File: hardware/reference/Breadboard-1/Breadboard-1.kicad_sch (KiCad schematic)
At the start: 59 parts, among them J1 Left, J2 Right, J3 ICSP, J4 USB_B_Micro, Q31 HSM0903, Q32 HSM0903, Q41 2N7002, Q42 2N7002, Q43 2N7002, U11 AMS1117-5.0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

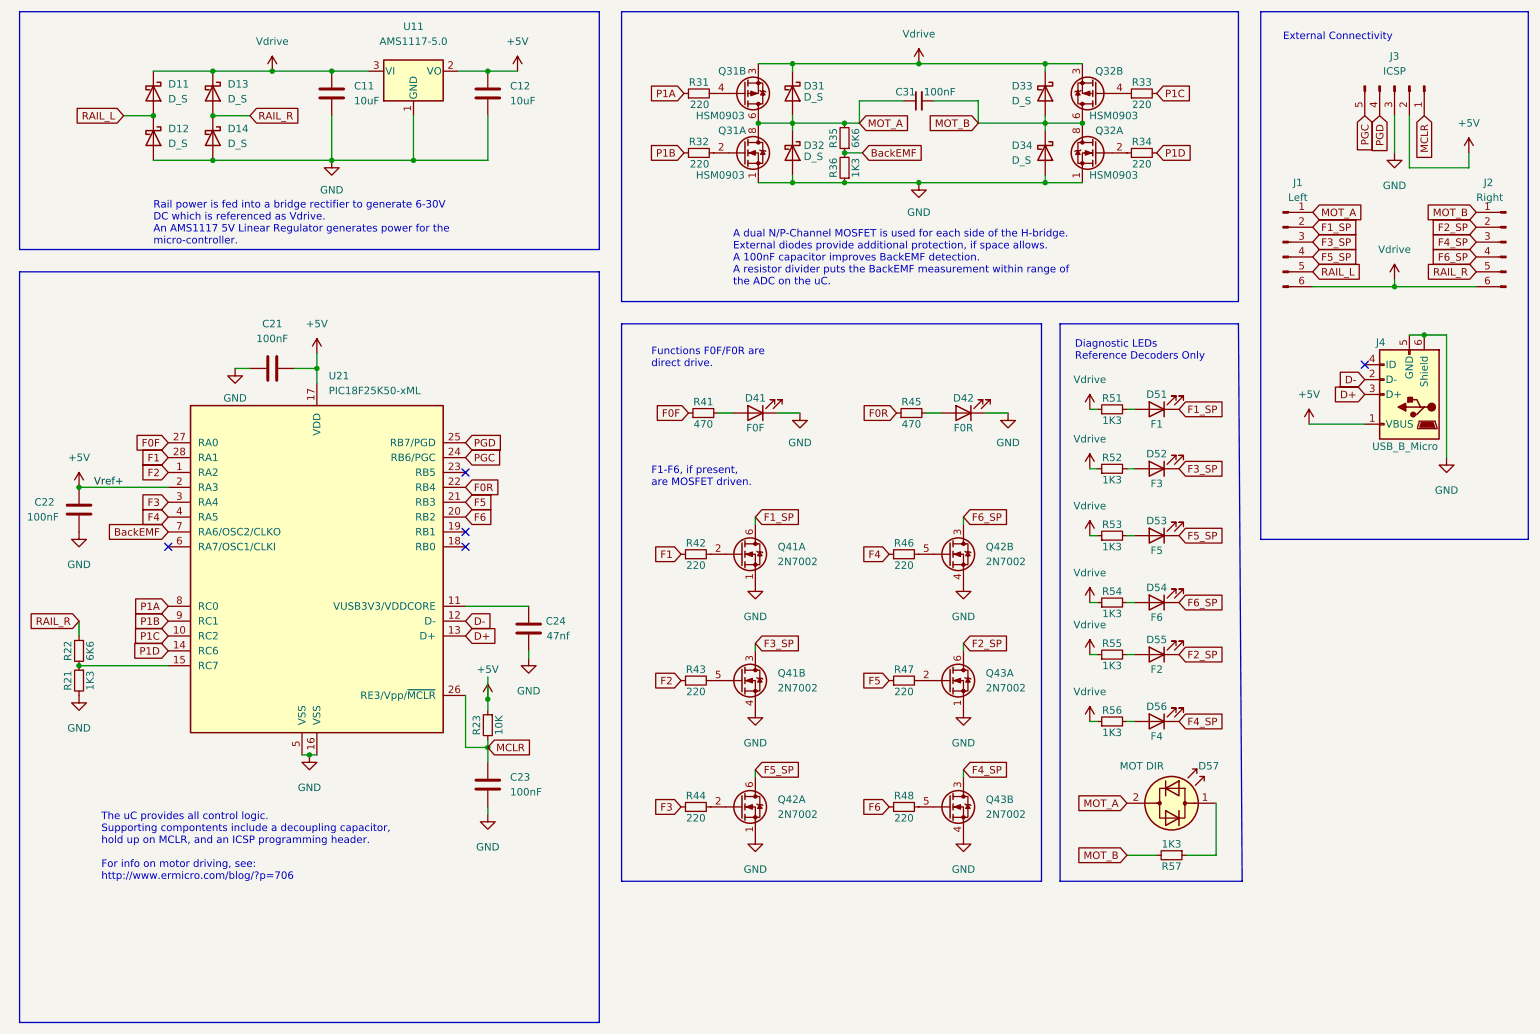
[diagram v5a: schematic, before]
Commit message: Chip selection update, new symbols, improved reference design.
Updated the chip selection document based on availability.

Added new symbols for the chips in the chip selection document.

Switched the reference design to an SSOP-20 package and improved the
layout in general.
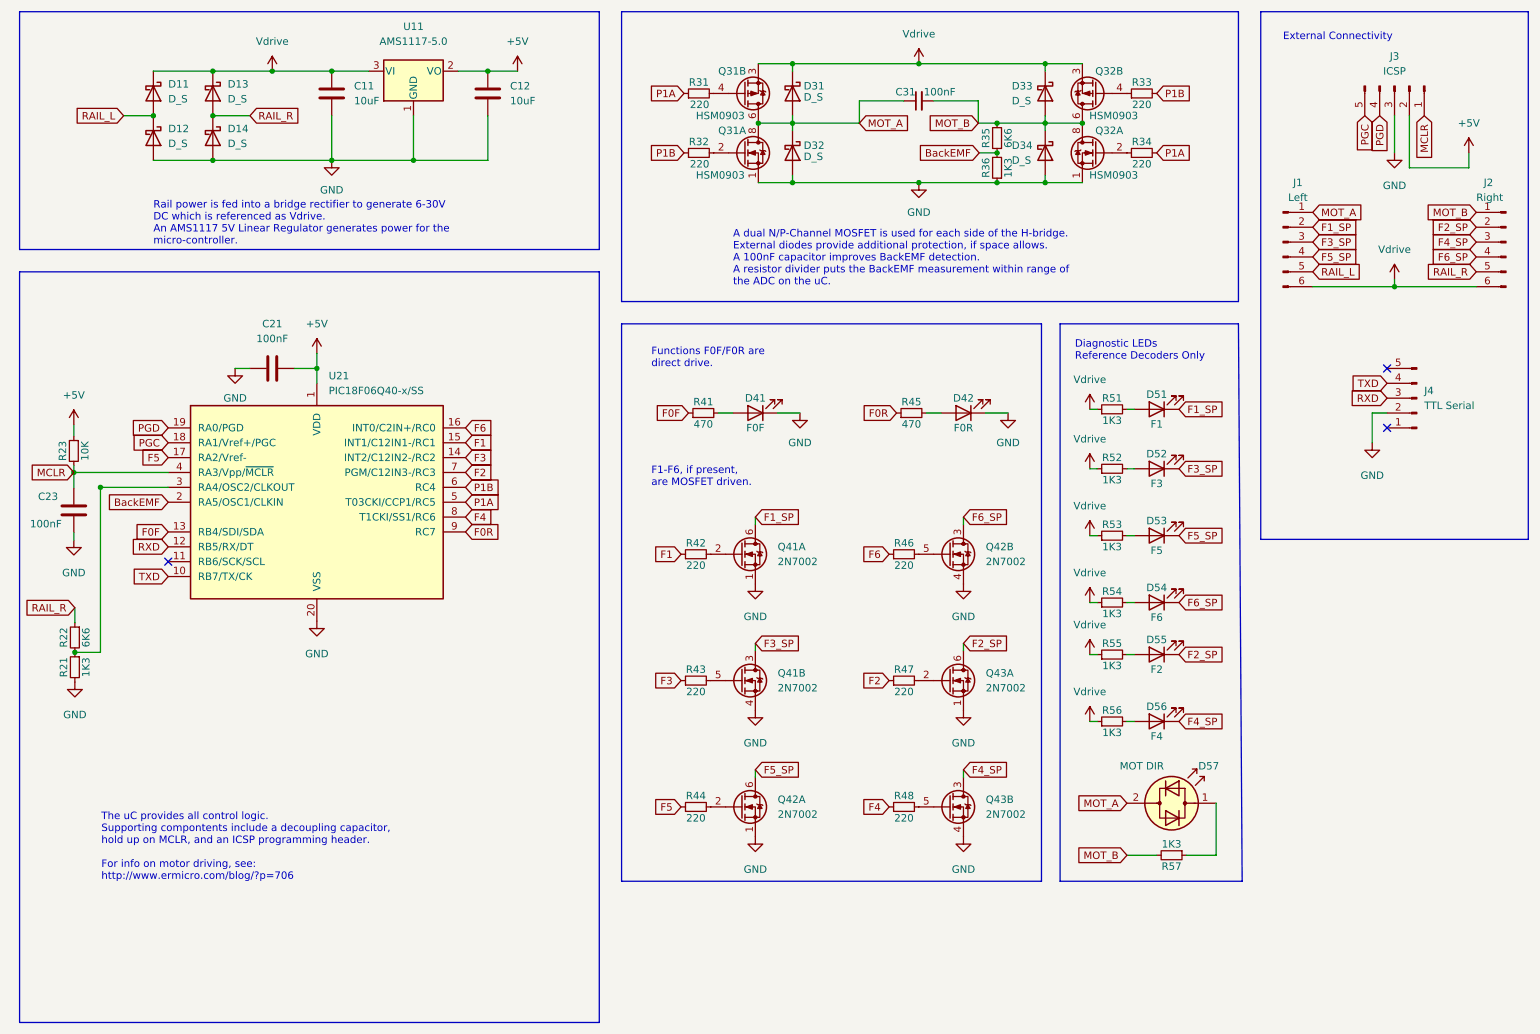
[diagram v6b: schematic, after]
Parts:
- removed C22: 100nF, Capacitor_SMD:C_0402_1005Metric, symbol Device:C
- removed C24: 47nf, Capacitor_SMD:C_0402_1005Metric, symbol Device:C
- removed J4: USB_B_Micro, Connector_USB:USB_Micro-B_Wuerth_629105150521, symbol Connector:USB_B_Micro
- removed U21: PIC18F25K50-xML, Package_DFN_QFN:QFN-28-1EP_6x6mm_P0.65mm_EP4.25x4.25mm, symbol MCU_Microchip_PIC18:PIC18F25K50-xML
- added J4: TTL Serial, Connector_PinSocket_2.54mm:PinSocket_1x05_P2.54mm_Vertical, symbol Connector:Conn_01x05_Male
- added U21: PIC18F06Q40-x/SS, Package_SO:SSOP-20_5.3x7.2mm_P0.65mm, symbol DCC Project Symbols:PIC18F06Q40-x/SS
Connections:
- net P1C is gone; now on net P1B: R33.2
- net P1D is gone; now on net P1A: R34.2
- net +5V: now also U21.1 (VDD)
- net BackEMF: now also U21.2 (RA5/OSC1/CLKIN)
- net F0F: now also U21.13 (RB4/SDI/SDA)
- net F0R: now also U21.9 (RC7)
- net F1: now also U21.15 (INT1/C12IN1-/RC1)
- net F2: now also R47.1, U21.7 (PGM/C12IN3-/RC3); no longer R43.1
- net F3: now also R43.1, U21.14 (INT2/C12IN2-/RC2); no longer R44.1
- net F4: now also R48.1, U21.8 (T1CKI/SS1/RC6); no longer R46.1
- net F5: now also R44.1, U21.17 (RA2/Vref-); no longer R47.1
- net F6: now also R46.1, U21.16 (INT0/C2IN+/RC0); no longer R48.1
- net GND: now also J4.2 (Pin_2), U21.20 (VSS)
- net MCLR: now also U21.4 (RA3/Vpp/~{MCLR})
- net MOT_A: no longer R35.2
- net MOT_B: now also R35.2
- net P1A: now also U21.5 (T03CKI/CCP1/RC5)
- net P1B: now also U21.6 (RC4)
- net PGC: now also U21.18 (RA1/Vref+/PGC)
- net PGD: now also U21.19 (RA0/PGD)
- net at R21.1, R22.2: now also U21.3 (RA4/OSC2/CLKOUT)
- new net RXD: J4.3 (Pin_3), U21.12 (RB5/RX/DT)
- new net TXD: J4.4 (Pin_4), U21.10 (RB7/TX/CK)
- no-connect marks 5 -> 3
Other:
- moved on the sheet: C23, R21, R22, R23, R35, R36

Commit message: Updated to the new processor and lots of board layout cleanup.
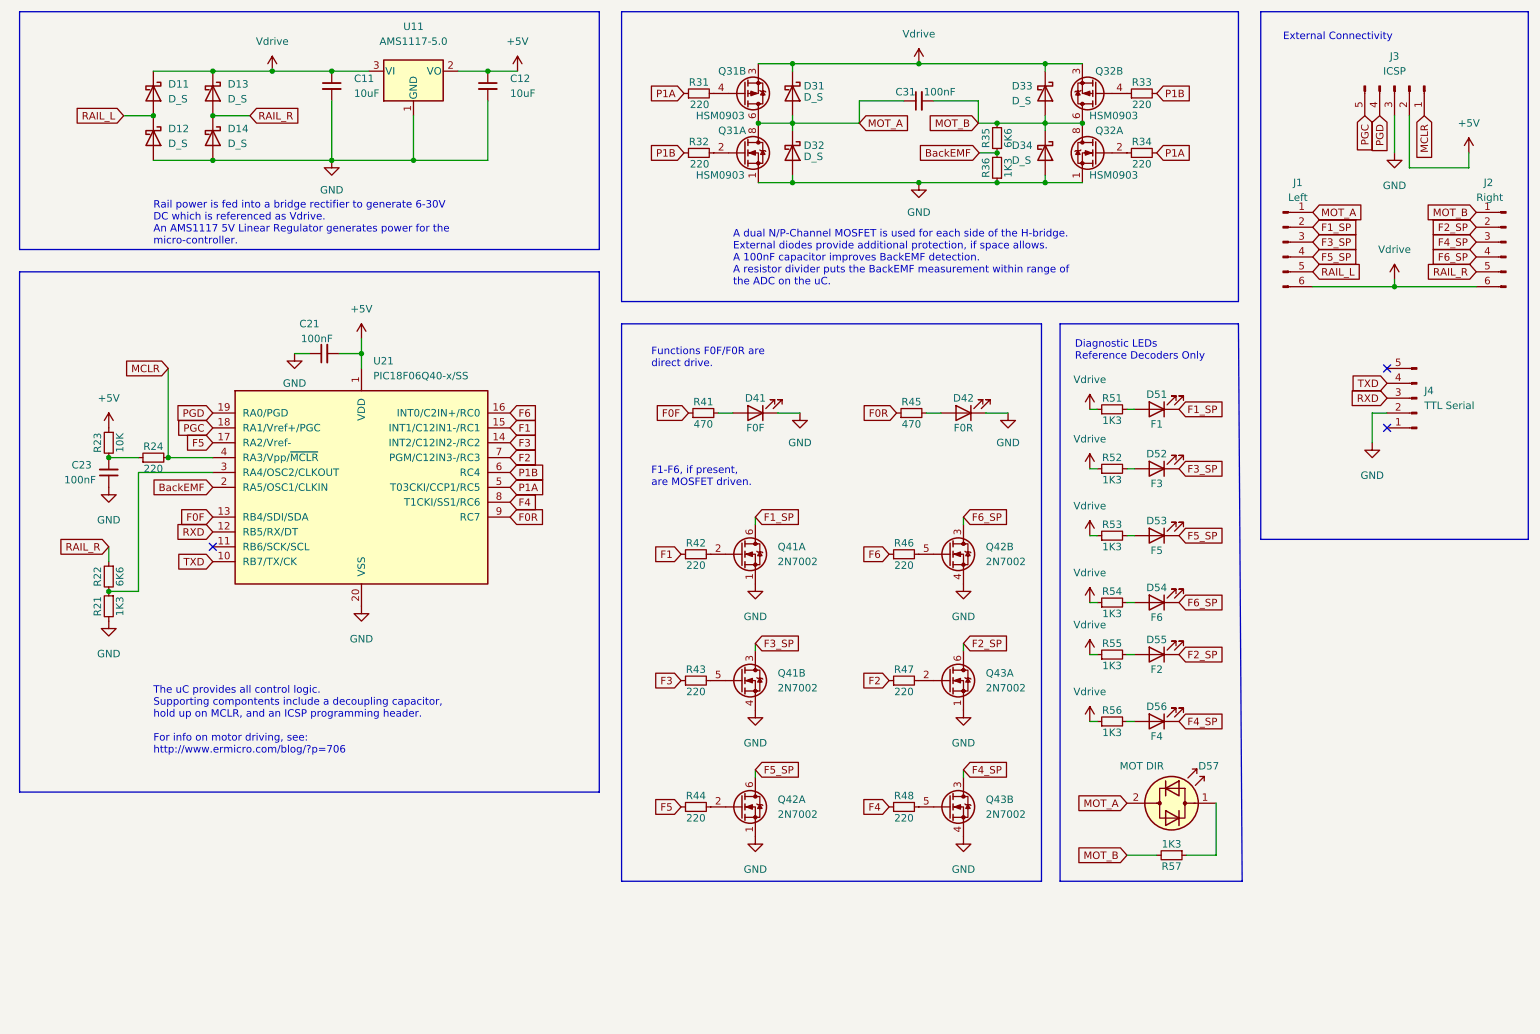
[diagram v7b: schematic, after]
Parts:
- added R24: 220, Resistor_SMD:R_0402_1005Metric, symbol Device:R_Small
- C11, C12, C21, C23: symbol Device:C -> Device:C_Small
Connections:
- net MCLR: now also R24.2; no longer C23.2, R23.2
- new net: C23.2, R23.2, R24.1
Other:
- moved on the sheet: C11, C12, C21, C23, R21, R22, R23, U21

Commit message: Position cleanup, better trace routing.
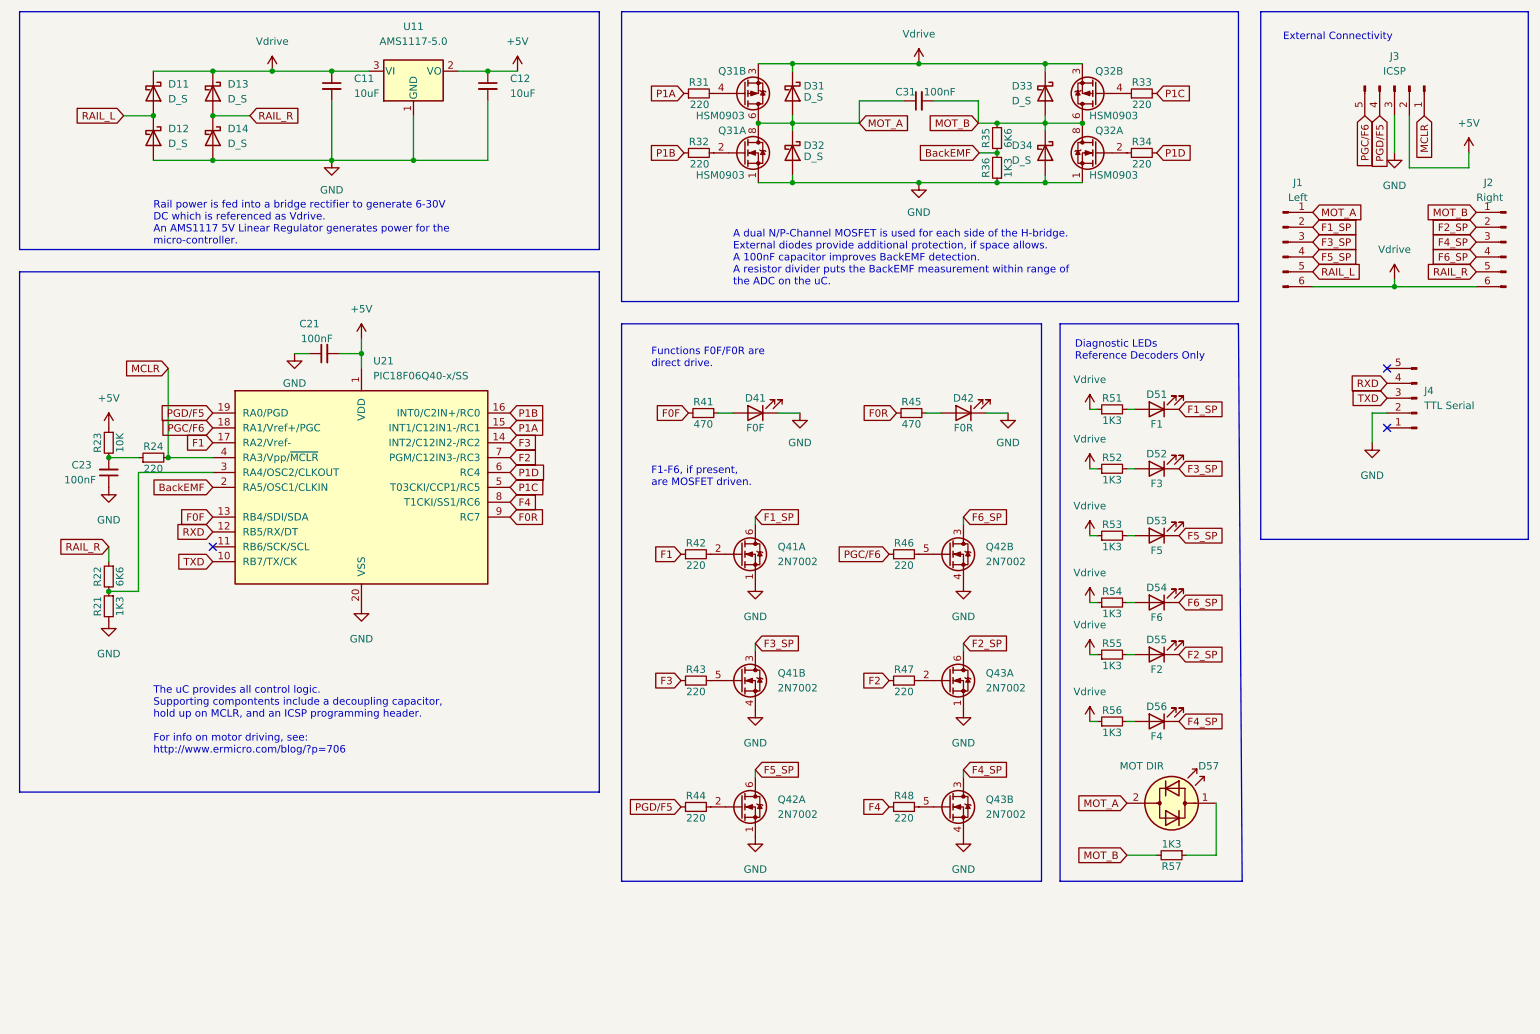
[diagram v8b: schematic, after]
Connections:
- net PGC is gone; now on net PGC/F6: J3.5 (Pin_5), U21.18 (RA1/Vref+/PGC)
- net PGD is gone; now on net PGD/F5: J3.4 (Pin_4), U21.19 (RA0/PGD)
- net F1: now also U21.17 (RA2/Vref-); no longer U21.15 (INT1/C12IN1-/RC1)
- net P1A: now also U21.15 (INT1/C12IN1-/RC1); no longer R34.2, U21.5 (T03CKI/CCP1/RC5)
- net P1B: now also U21.16 (INT0/C2IN+/RC0); no longer R33.2, U21.6 (RC4)
- net RXD: now also J4.4 (Pin_4); no longer J4.3 (Pin_3)
- net TXD: now also J4.3 (Pin_3); no longer J4.4 (Pin_4)
- net F5 renamed PGD/F5
- net PGD/F5: no longer U21.17 (RA2/Vref-)
- net F6 renamed PGC/F6
- net PGC/F6: no longer U21.16 (INT0/C2IN+/RC0)
- new net P1C: R33.2, U21.5 (T03CKI/CCP1/RC5)
- new net P1D: R34.2, U21.6 (RC4)
